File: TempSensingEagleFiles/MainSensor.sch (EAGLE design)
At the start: 14 parts, among them U3 MLX90614_

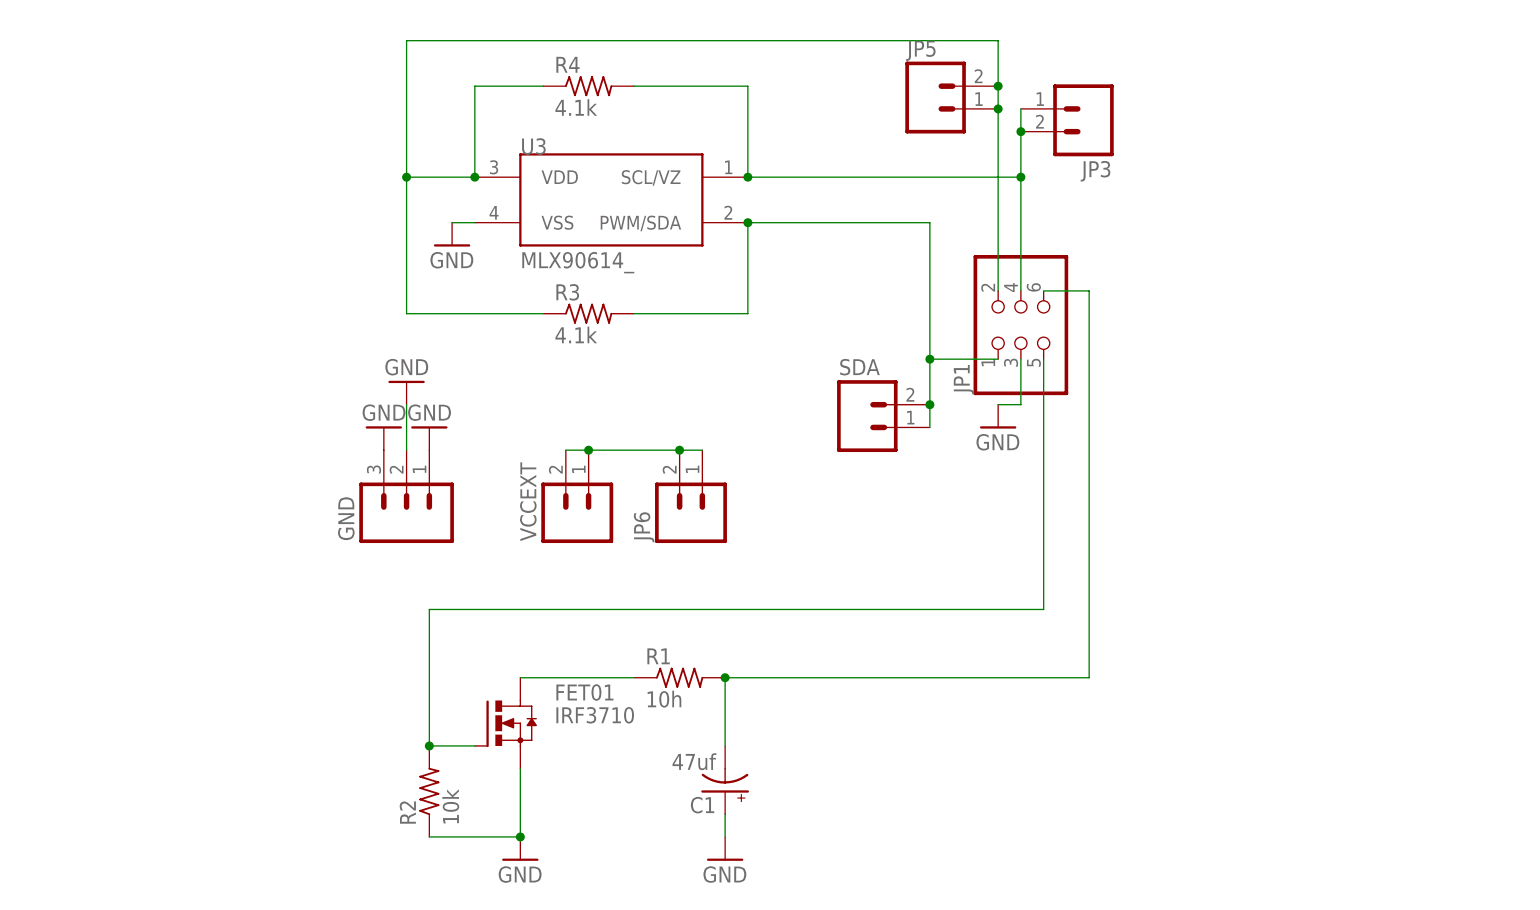
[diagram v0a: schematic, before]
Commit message: worked on Eagle Files
Added 1 Sensor and Main board
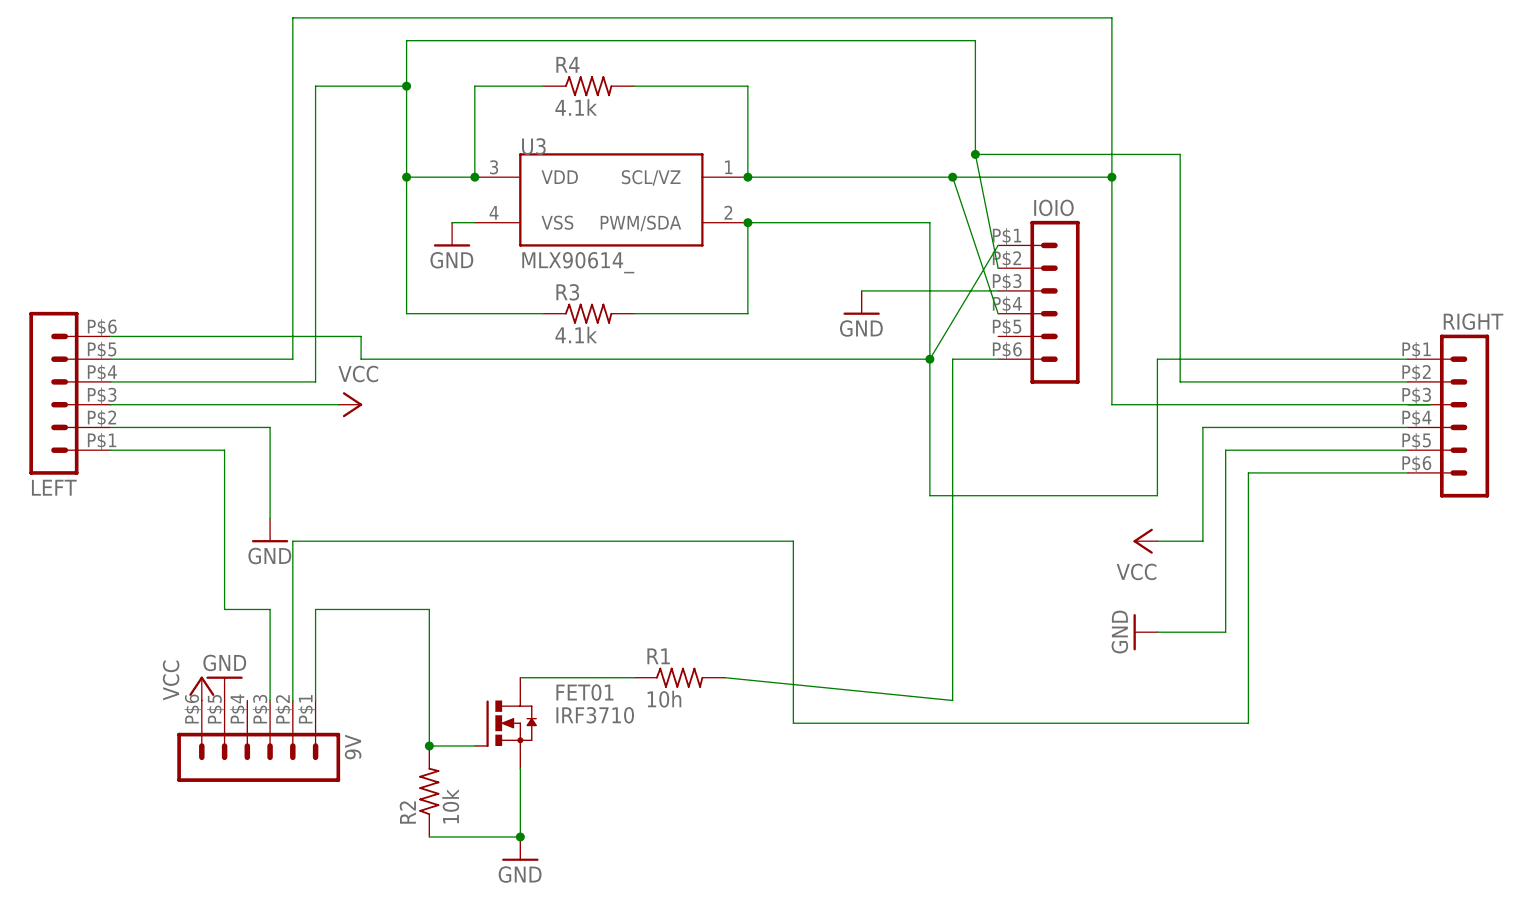
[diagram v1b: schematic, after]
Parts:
- removed C1: 47uf, rcl:CPOL-USE2,5-6E
- removed GND: (no value), SparkFun-Connectors:M03LONGPADS
- removed JP1: (no value), SparkFun-Connectors:PINHD-2X3
- removed JP3, JP5, JP6, SDA, VCCEXT: (no value), SparkFun-Connectors:M02LOCK_LONGPADS
- added 9V, IOIO, LEFT, RIGHT: (no value), con-molex-micro-fit-3_0:HEADER_POS6_43045-0600
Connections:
- new net N$4: 9V.3, LEFT.1
- new net VCC: 9V.6, LEFT.3, RIGHT.4
- net GND: now also IOIO.3, LEFT.2, RIGHT.5; no longer C1.+, GND.1, GND.2, GND.3, JP1.3
- net N$1: now also 9V.2, RIGHT.6; no longer JP6.1, JP6.2, VCCEXT.1, VCCEXT.2
- net N$15: now also IOIO.4, LEFT.5; no longer JP1.4, JP3.1, JP3.2
- net N$16: now also IOIO.1, LEFT.6, RIGHT.1; no longer JP1.1, SDA.1, SDA.2
- net N$18: now also 9V.1; no longer JP1.5
- net N$3: now also IOIO.6; no longer C1.-, JP1.6
- net VCC3: now also IOIO.2, LEFT.4, RIGHT.2; no longer JP1.2, JP5.1, JP5.2

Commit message: STABLE: Added better threading
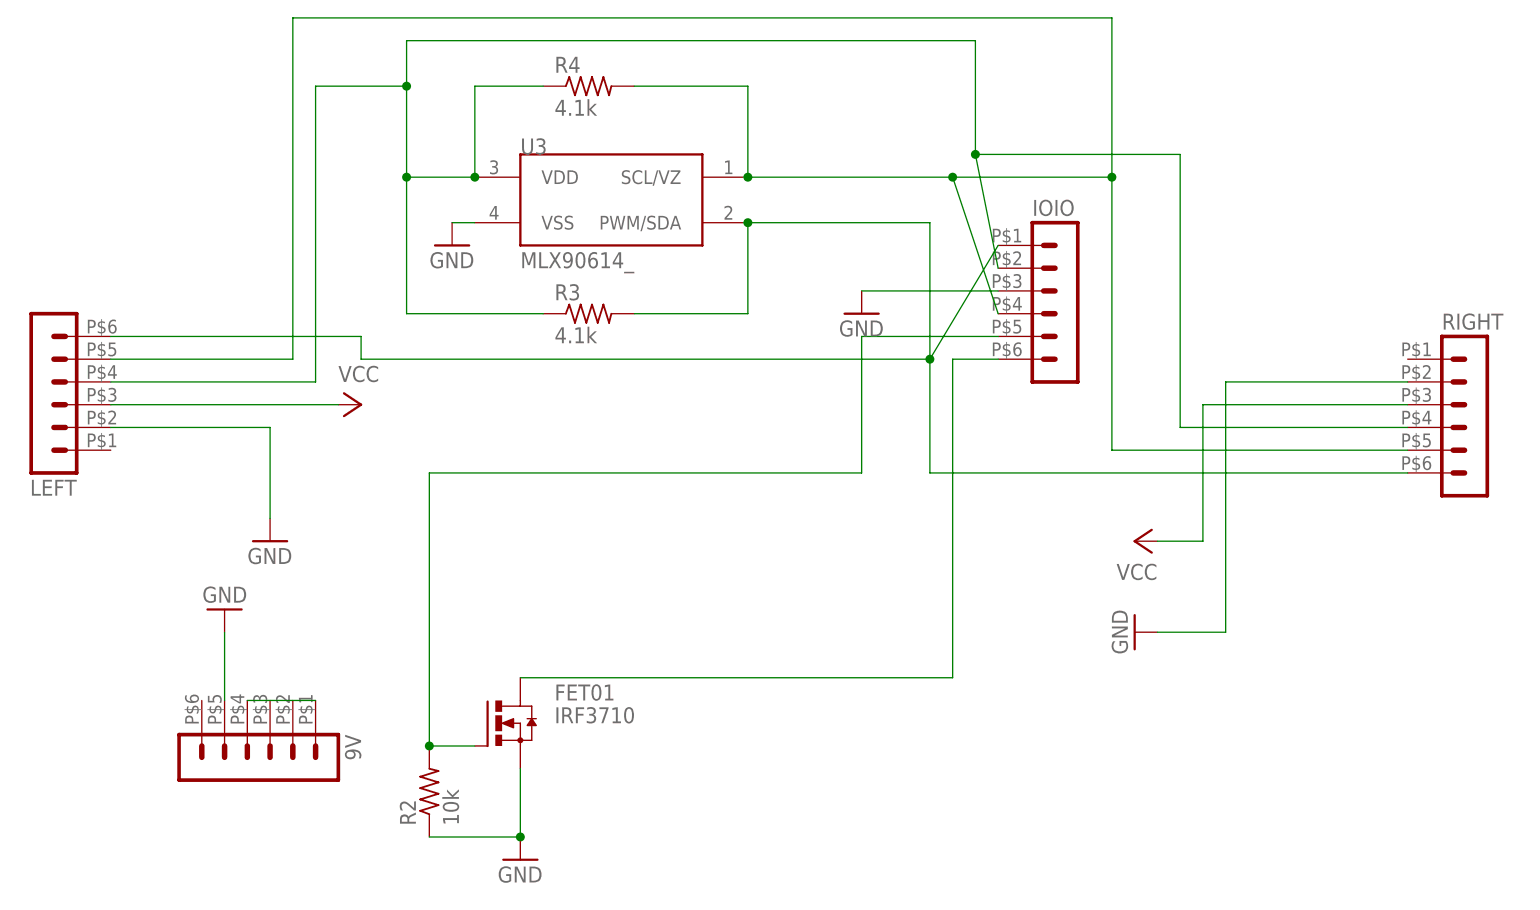
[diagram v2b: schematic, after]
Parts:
- removed R1: 10h, rcl:R-US_0207/7
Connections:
- removed net N$15: IOIO.4, LEFT.5, R4.2, U3.SCL/VZ
- removed net N$16: IOIO.1, LEFT.6, R3.2, RIGHT.1, U3.PWM/SDA
- removed net N$18: 9V.1, FET01.G, R2.2
- removed net N$2: FET01.D, R1.1
- removed net N$3: IOIO.6, R1.2
- removed net N$4: 9V.3, LEFT.1
- removed net VCC3: IOIO.2, LEFT.4, R3.1, R4.1, RIGHT.2, U3.VDD
- new net 3.3V: IOIO.2, LEFT.4, R3.1, R4.1, RIGHT.4, U3.VDD
- new net IOIOPIN: FET01.G, IOIO.5, R2.2
- new net SCL: IOIO.4, LEFT.5, R4.2, RIGHT.5, U3.SCL/VZ
- new net SDA: IOIO.1, LEFT.6, R3.2, RIGHT.6, U3.PWM/SDA
- new net VIB: FET01.D, IOIO.6
- net GND: now also 9V.5, RIGHT.2; no longer RIGHT.5
- net N$1: now also 9V.1, 9V.3, 9V.4; no longer RIGHT.6
- net VCC: now also RIGHT.3; no longer 9V.6, RIGHT.4
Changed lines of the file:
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@@
 </variantdefs>
 <classes>
-<class number="0" name="default" width="0.508" drill="0.508">
+<class number="0" name="default" width="0.6096" drill="1.27">
 <clearance class="0" value="0.508"/>
 </class>
@@
 <parts>
 <part name="FET01" library="transistor-power" deviceset="IRF3704" device="" value="IRF3710"/>
-<part name="R1" library="rcl" deviceset="R-US_" device="0207/7" value="10h"/>
 <part name="R2" library="rcl" deviceset="R-US_" device="0207/7" value="10k"/>
 <part name="U3" library="SparkFun-Sensors" deviceset="MLX90614" device="_"/>
@@
 <part name="MOTOR9V2" library="supply1" deviceset="VCC" device=""/>
 <part name="9V" library="con-molex-micro-fit-3_0" deviceset="HEADER_POS6_?" device="43045-0600"/>
-<part name="MOTOR9V3" library="supply1" deviceset="VCC" device=""/>
 <part name="GND7" library="supply1" deviceset="GND" device=""/>
 <part name="RIGHT" library="con-molex-micro-fit-3_0" deviceset="HEADER_POS6_?" device="43045-0600"/>
@@
 <instances>
 <instance part="FET01" gate="G$1" x="142.24" y="48.26"/>
-<instance part="R1" gate="G$1" x="162.56" y="53.34"/>
 <instance part="R2" gate="G$1" x="134.62" y="40.64" rot="R90"/>
 <instance part="U3" gate="G$1" x="154.94" y="106.68"/>
@@
 <instance part="MOTOR9V2" gate="VCC" x="127" y="83.82" rot="R270"/>
 <instance part="9V" gate="G$1" x="114.3" y="45.72" rot="R270"/>
-<instance part="MOTOR9V3" gate="VCC" x="109.22" y="53.34"/>
-<instance part="GND7" gate="1" x="111.76" y="53.34" rot="R180"/>
+<instance part="GND7" gate="1" x="111.76" y="60.96" rot="R180"/>
 <instance part="RIGHT" gate="G$1" x="248.92" y="81.28"/>
 <instance part="LEFT" gate="G$1" x="93.98" y="86.36" rot="R180"/>
@@
 </busses>
 <nets>
-<net name="N$15" class="0">
+<net name="SCL" class="0">
 <segment>
 <pinref part="R4" gate="G$1" pin="2"/>
@@
 <wire x1="198.12" y1="93.98" x2="193.04" y2="109.22" width="0.1524" layer="91"/>
 <wire x1="193.04" y1="109.22" x2="210.82" y2="109.22" width="0.1524" layer="91"/>
-<wire x1="210.82" y1="109.22" x2="210.82" y2="83.82" width="0.1524" layer="91"/>
+<wire x1="210.82" y1="109.22" x2="210.82" y2="78.74" width="0.1524" layer="91"/>
 <wire x1="210.82" y1="109.22" x2="210.82" y2="127" width="0.1524" layer="91"/>
 <wire x1="210.82" y1="127" x2="119.38" y2="127" width="0.1524" layer="91"/>
@@
 <pinref part="LEFT" gate="G$1" pin="5"/>
 <wire x1="119.38" y1="88.9" x2="99.06" y2="88.9" width="0.1524" layer="91"/>
-<wire x1="210.82" y1="83.82" x2="246.38" y2="83.82" width="0.1524" layer="91"/>
-</segment>
-</net>
-<net name="N$16" class="0">
+<pinref part="RIGHT" gate="G$1" pin="5"/>
+<wire x1="210.82" y1="78.74" x2="243.84" y2="78.74" width="0.1524" layer="91"/>
+</segment>
+</net>
+<net name="SDA" class="0">
 <segment>
 <pinref part="U3" gate="G$1" pin="PWM/SDA"/>
@@
 <wire x1="127" y1="91.44" x2="127" y2="88.9" width="0.1524" layer="91"/>
 <wire x1="127" y1="88.9" x2="190.5" y2="88.9" width="0.1524" layer="91"/>
-<wire x1="190.5" y1="88.9" x2="190.5" y2="73.66" width="0.1524" layer="91"/>
-<wire x1="190.5" y1="73.66" x2="215.9" y2="73.66" width="0.1524" layer="91"/>
-<wire x1="215.9" y1="73.66" x2="215.9" y2="88.9" width="0.1524" layer="91"/>
+<wire x1="190.5" y1="88.9" x2="190.5" y2="76.2" width="0.1524" layer="91"/>
 <junction x="190.5" y="88.9"/>
 <pinref part="LEFT" gate="G$1" pin="6"/>
-<pinref part="RIGHT" gate="G$1" pin="1"/>
-<wire x1="215.9" y1="88.9" x2="243.84" y2="88.9" width="0.1524" layer="91"/>
-</segment>
-</net>
-<net name="N$18" class="0">
-<segment>
-<pinref part="FET01" gate="G$1" pin="G"/>
-<pinref part="R2" gate="G$1" pin="2"/>
-<wire x1="134.62" y1="45.72" x2="139.7" y2="45.72" width="0.1524" layer="91"/>
-<wire x1="134.62" y1="60.96" x2="134.62" y2="45.72" width="0.1524" layer="91"/>
-<junction x="134.62" y="45.72"/>
-<pinref part="9V" gate="G$1" pin="1"/>
-<wire x1="134.62" y1="60.96" x2="121.92" y2="60.96" width="0.1524" layer="91"/>
-<wire x1="121.92" y1="60.96" x2="121.92" y2="50.8" width="0.1524" layer="91"/>
+<pinref part="RIGHT" gate="G$1" pin="6"/>
+<wire x1="190.5" y1="76.2" x2="243.84" y2="76.2" width="0.1524" layer="91"/>
 </segment>
 </net>
@@
 <segment>
 <pinref part="GND2" gate="1" pin="GND"/>
-<wire x1="223.52" y1="78.74" x2="223.52" y2="58.42" width="0.1524" layer="91"/>
+<wire x1="223.52" y1="86.36" x2="223.52" y2="58.42" width="0.1524" layer="91"/>
 <wire x1="223.52" y1="58.42" x2="215.9" y2="58.42" width="0.1524" layer="91"/>
-<pinref part="RIGHT" gate="G$1" pin="5"/>
-<wire x1="223.52" y1="78.74" x2="243.84" y2="78.74" width="0.1524" layer="91"/>
-</segment>
-</net>
-<net name="N$2" class="0">
-<segment>
-<pinref part="FET01" gate="G$1" pin="D"/>
-<pinref part="R1" gate="G$1" pin="1"/>
-<wire x1="157.48" y1="53.34" x2="144.78" y2="53.34" width="0.1524" layer="91"/>
-</segment>
-</net>
-<net name="VCC3" class="0">
+<pinref part="RIGHT" gate="G$1" pin="2"/>
+<wire x1="223.52" y1="86.36" x2="243.84" y2="86.36" width="0.1524" layer="91"/>
+</segment>
+<segment>
+<pinref part="GND7" gate="1" pin="GND"/>
+<pinref part="9V" gate="G$1" pin="5"/>
+<wire x1="111.76" y1="58.42" x2="111.76" y2="50.8" width="0.1524" layer="91"/>
+</segment>
+</net>
+<net name="3.3V" class="0">
 <segment>
 <pinref part="U3" gate="G$1" pin="VDD"/>
@@
 <wire x1="121.92" y1="119.38" x2="121.92" y2="86.36" width="0.1524" layer="91"/>
 <wire x1="195.58" y1="111.76" x2="218.44" y2="111.76" width="0.1524" layer="91"/>
-<wire x1="218.44" y1="111.76" x2="218.44" y2="86.36" width="0.1524" layer="91"/>
+<wire x1="218.44" y1="111.76" x2="218.44" y2="81.28" width="0.1524" layer="91"/>
 <junction x="132.08" y="119.38"/>
 <junction x="195.58" y="111.76"/>
 <pinref part="LEFT" gate="G$1" pin="4"/>
 <wire x1="121.92" y1="86.36" x2="99.06" y2="86.36" width="0.1524" layer="91"/>
-<pinref part="RIGHT" gate="G$1" pin="2"/>
-<wire x1="218.44" y1="86.36" x2="243.84" y2="86.36" width="0.1524" layer="91"/>
-</segment>
-</net>
-<net name="N$3" class="0">
-<segment>
-<pinref part="R1" gate="G$1" pin="2"/>
-<wire x1="167.64" y1="53.34" x2="193.04" y2="50.8" width="0.1524" layer="91"/>
-<wire x1="193.04" y1="50.8" x2="193.04" y2="88.9" width="0.1524" layer="91"/>
+<pinref part="RIGHT" gate="G$1" pin="4"/>
+<wire x1="218.44" y1="81.28" x2="243.84" y2="81.28" width="0.1524" layer="91"/>
+</segment>
+</net>
+<net name="VIB" class="0">
+<segment>
+<wire x1="144.78" y1="53.34" x2="193.04" y2="53.34" width="0.1524" layer="91"/>
+<wire x1="193.04" y1="53.34" x2="193.04" y2="88.9" width="0.1524" layer="91"/>
 <pinref part="IOIO" gate="G$1" pin="6"/>
 <wire x1="193.04" y1="88.9" x2="198.12" y2="88.9" width="0.1524" layer="91"/>
+<pinref part="FET01" gate="G$1" pin="D"/>
 </segment>
 </net>
 <net name="VCC" class="0">
 <segment>
-<wire x1="220.98" y1="81.28" x2="220.98" y2="68.58" width="0.1524" layer="91"/>
+<wire x1="220.98" y1="83.82" x2="220.98" y2="68.58" width="0.1524" layer="91"/>
 <pinref part="MOTOR9V1" gate="VCC" pin="VCC"/>
 <wire x1="220.98" y1="68.58" x2="215.9" y2="68.58" width="0.1524" layer="91"/>
-<pinref part="RIGHT" gate="G$1" pin="4"/>
-<wire x1="220.98" y1="81.28" x2="243.84" y2="81.28" width="0.1524" layer="91"/>
+<pinref part="RIGHT" gate="G$1" pin="3"/>
+<wire x1="220.98" y1="83.82" x2="243.84" y2="83.82" width="0.1524" layer="91"/>
 </segment>
 <segment>
@@
 <wire x1="124.46" y1="83.82" x2="99.06" y2="83.82" width="0.1524" layer="91"/>
 </segment>
-<segment>
-<pinref part="9V" gate="G$1" pin="6"/>
-<pinref part="MOTOR9V3" gate="VCC" pin="VCC"/>
+</net>
+<net name="IOIOPIN" class="0">
+<segment>
+<pinref part="FET01" gate="G$1" pin="G"/>
+<pinref part="R2" gate="G$1" pin="2"/>
+<wire x1="134.62" y1="45.72" x2="139.7" y2="45.72" width="0.1524" layer="91"/>
+<junction x="134.62" y="45.72"/>
+<pinref part="IOIO" gate="G$1" pin="5"/>
+<wire x1="198.12" y1="91.44" x2="182.88" y2="91.44" width="0.1524" layer="91"/>
+<wire x1="182.88" y1="91.44" x2="182.88" y2="76.2" width="0.1524" layer="91"/>
+<wire x1="182.88" y1="76.2" x2="134.62" y2="76.2" width="0.1524" layer="91"/>
+<wire x1="134.62" y1="76.2" x2="134.62" y2="45.72" width="0.1524" layer="91"/>
 </segment>
 </net>
 <net name="N$1" class="0">
 <segment>
-<wire x1="226.06" y1="76.2" x2="226.06" y2="48.26" width="0.1524" layer="91"/>
-<wire x1="226.06" y1="48.26" x2="175.26" y2="48.26" width="0.1524" layer="91"/>
-<wire x1="175.26" y1="48.26" x2="175.26" y2="68.58" width="0.1524" layer="91"/>
+<pinref part="9V" gate="G$1" pin="4"/>
+<pinref part="9V" gate="G$1" pin="3"/>
 <pinref part="9V" gate="G$1" pin="2"/>
-<wire x1="175.26" y1="68.58" x2="119.38" y2="68.58" width="0.1524" layer="91"/>
-<wire x1="119.38" y1="68.58" x2="119.38" y2="50.8" width="0.1524" layer="91"/>
-<pinref part="RIGHT" gate="G$1" pin="6"/>
-<wire x1="226.06" y1="76.2" x2="243.84" y2="76.2" width="0.1524" layer="91"/>
-</segment>
-</net>
-<net name="N$4" class="0">
-<segment>
-<wire x1="111.76" y1="78.74" x2="111.76" y2="60.96" width="0.1524" layer="91"/>
-<pinref part="9V" gate="G$1" pin="3"/>
-<wire x1="111.76" y1="60.96" x2="116.84" y2="60.96" width="0.1524" layer="91"/>
-<wire x1="116.84" y1="60.96" x2="116.84" y2="50.8" width="0.1524" layer="91"/>
-<pinref part="LEFT" gate="G$1" pin="1"/>
-<wire x1="111.76" y1="78.74" x2="99.06" y2="78.74" width="0.1524" layer="91"/>
-</segment>
-</net>
+<pinref part="9V" gate="G$1" pin="1"/>
+<wire x1="121.92" y1="50.8" x2="119.38" y2="50.8" width="0.1524" layer="91"/>
+<wire x1="119.38" y1="50.8" x2="116.84" y2="50.8" width="0.1524" layer="91"/>
+<wire x1="116.84" y1="50.8" x2="114.3" y2="50.8" width="0.1524" layer="91"/>
+</segment>
+</net>
